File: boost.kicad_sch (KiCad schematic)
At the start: 0 parts

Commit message: Added some text in the subsheets to outline what needs to be added inside of each subsheet
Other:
- note added: "TODO: - Boost a variable voltage from the supercaps to a constant +24V - Figure out line & load regulation - Be able to shut off the boost converter with an active low signal"
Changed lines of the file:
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@@
 		(comment 1 "Robomaster")
 	)
+	(text "TODO:\n- Boost a variable voltage from the supercaps to a constant +24V\n  - Figure out line & load regulation\n- Be able to shut off the boost converter with an active low signal"
+		(exclude_from_sim no)
+		(at 125.095 90.805 0)
+		(effects
+			(font
+				(size 1.27 1.27)
+			)
+			(justify left top)
+		)
+	)
 )

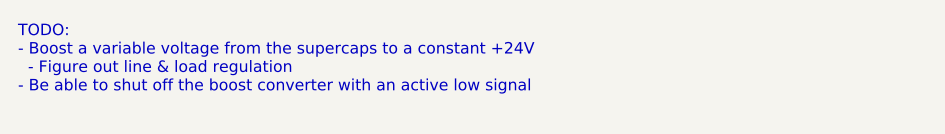
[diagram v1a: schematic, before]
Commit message: Add note about synchronous boost/buck needed
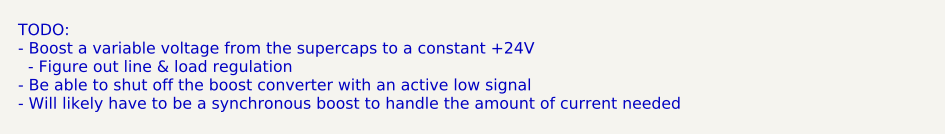
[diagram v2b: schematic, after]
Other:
- note added: "TODO: - Boost a variable voltage from the supercaps to a constant +24V - Figure out line & load regulation - Be able to shut off the boost converter with an active low signal - Will likely have to be a synchronous boost to handle the amount of current needed"
- note removed: "TODO: - Boost a variable voltage from the supercaps to a constant +24V - Figure out line & load regulation - Be able to shut off the boost converter with an active low signal"
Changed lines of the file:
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@@
 		(comment 1 "Robomaster")
 	)
-	(text "TODO:\n- Boost a variable voltage from the supercaps to a constant +24V\n  - Figure out line & load regulation\n- Be able to shut off the boost converter with an active low signal"
+	(text "TODO:\n- Boost a variable voltage from the supercaps to a constant +24V\n  - Figure out line & load regulation\n- Be able to shut off the boost converter with an active low signal\n- Will likely have to be a synchronous boost to handle the amount of current needed"
 		(exclude_from_sim no)
 		(at 125.095 90.805 0)

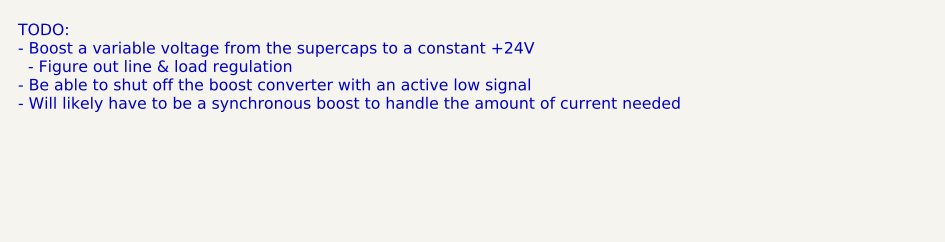
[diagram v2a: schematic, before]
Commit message: Added in & out data from each subsheet
For more details, please contact @leftisttachyon on Discord
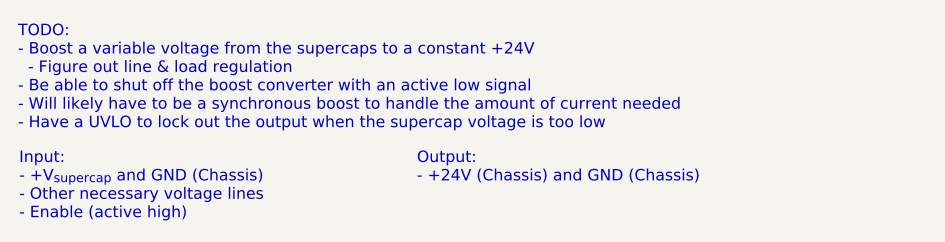
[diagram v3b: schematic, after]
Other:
- note added: "Input: - +V_{supercap} and GND (Chassis) - Other necessary voltage lines - Enable (active high)"
- note added: "Output: - +24V (Chassis) and GND (Chassis)"
- note added: "TODO: - Boost a variable voltage from the supercaps to a constant +24V - Figure out line & load regulation - Be able to shut off the boost converter with an active low signal - Will likely have to be a synchronous boost to handle the amount of current needed - Have a UVLO to lock out the output when the supercap voltage is too low"
- note removed: "TODO: - Boost a variable voltage from the supercaps to a constant +24V - Figure out line & load regulation - Be able to shut off the boost converter with an active low signal - Will likely have to be a synchronous boost to handle the amount of current needed"
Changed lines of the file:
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@@
 		(comment 1 "Robomaster")
 	)
-	(text "TODO:\n- Boost a variable voltage from the supercaps to a constant +24V\n  - Figure out line & load regulation\n- Be able to shut off the boost converter with an active low signal\n- Will likely have to be a synchronous boost to handle the amount of current needed"
+	(text "TODO:\n- Boost a variable voltage from the supercaps to a constant +24V\n  - Figure out line & load regulation\n- Be able to shut off the boost converter with an active low signal\n- Will likely have to be a synchronous boost to handle the amount of current needed\n- Have a UVLO to lock out the output when the supercap voltage is too low"
 		(exclude_from_sim no)
 		(at 125.095 90.805 0)
 		(effects
 			(font
+				(size 1.27 1.27)
+			)
+			(justify left top)
+		)
+	)
+	(text "Output:\n- +24V (Chassis) and GND (Chassis)"
+		(exclude_from_sim no)
+		(at 169.418 104.902 0)
+		(effects
+			(font
+				(size 1.27 1.27)
+			)
+			(justify left top)
+		)
+	)
+	(text "Input:\n- +V_{supercap} and GND (Chassis)\n- Other necessary voltage lines\n- Enable (active high)"
+		(exclude_from_sim no)
+		(at 125.222 104.902 0)
+		(effects
+			(font

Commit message: Completed first version of housekeeping supplies
+5V and +3V3 from mini PC +24V
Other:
- company: UT Stampede -> UT Robomaster
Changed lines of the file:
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@@
 	(paper "A4")
 	(title_block
-		(date "2024-10-18")
+		(date "2024-11-15")
 		(rev "1")
-		(company "UT Stampede")
+		(company "UT Robomaster")
 		(comment 1 "Robomaster")
 	)

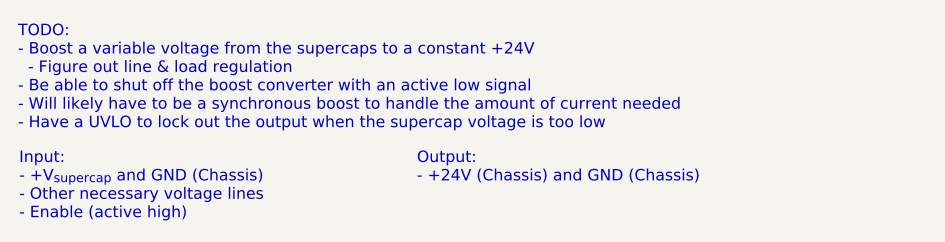
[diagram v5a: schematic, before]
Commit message: Updated sheet dates & added new subsheets for parts I forgot to include
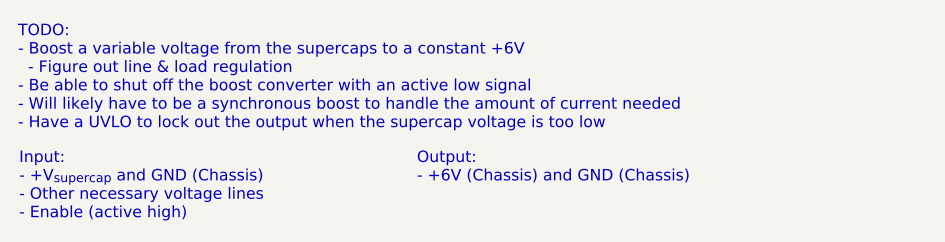
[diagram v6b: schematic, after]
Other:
- note added: "Output: - +6V (Chassis) and GND (Chassis)"
- note added: "TODO: - Boost a variable voltage from the supercaps to a constant +6V - Figure out line & load regulation - Be able to shut off the boost converter with an active low signal - Will likely have to be a synchronous boost to handle the amount of current needed - Have a UVLO to lock out the output when the supercap voltage is too low"
- note removed: "Output: - +24V (Chassis) and GND (Chassis)"
- note removed: "TODO: - Boost a variable voltage from the supercaps to a constant +24V - Figure out line & load regulation - Be able to shut off the boost converter with an active low signal - Will likely have to be a synchronous boost to handle the amount of current needed - Have a UVLO to lock out the output when the supercap voltage is too low"
- title: (none) -> Output Boost (Stage 1)
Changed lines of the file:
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@@
 	(paper "A4")
 	(title_block
-		(date "2024-12-06")
+		(title "Output Boost (Stage 1)")
+		(date "2025-02-12")
 		(rev "1")
 		(company "UT Robomaster")
 		(comment 1 "Robomaster")
 	)
-	(text "TODO:\n- Boost a variable voltage from the supercaps to a constant +24V\n  - Figure out line & load regulation\n- Be able to shut off the boost converter with an active low signal\n- Will likely have to be a synchronous boost to handle the amount of current needed\n- Have a UVLO to lock out the output when the supercap voltage is too low"
+	(text "TODO:\n- Boost a variable voltage from the supercaps to a constant +6V\n  - Figure out line & load regulation\n- Be able to shut off the boost converter with an active low signal\n- Will likely have to be a synchronous boost to handle the amount of current needed\n- Have a UVLO to lock out the output when the supercap voltage is too low"
 		(exclude_from_sim no)
 		(at 125.095 90.805 0)
@@
 		)
 	)
-	(text "Output:\n- +24V (Chassis) and GND (Chassis)"
+	(text "Output:\n- +6V (Chassis) and GND (Chassis)"
 		(exclude_from_sim no)
 		(at 169.418 104.902 0)

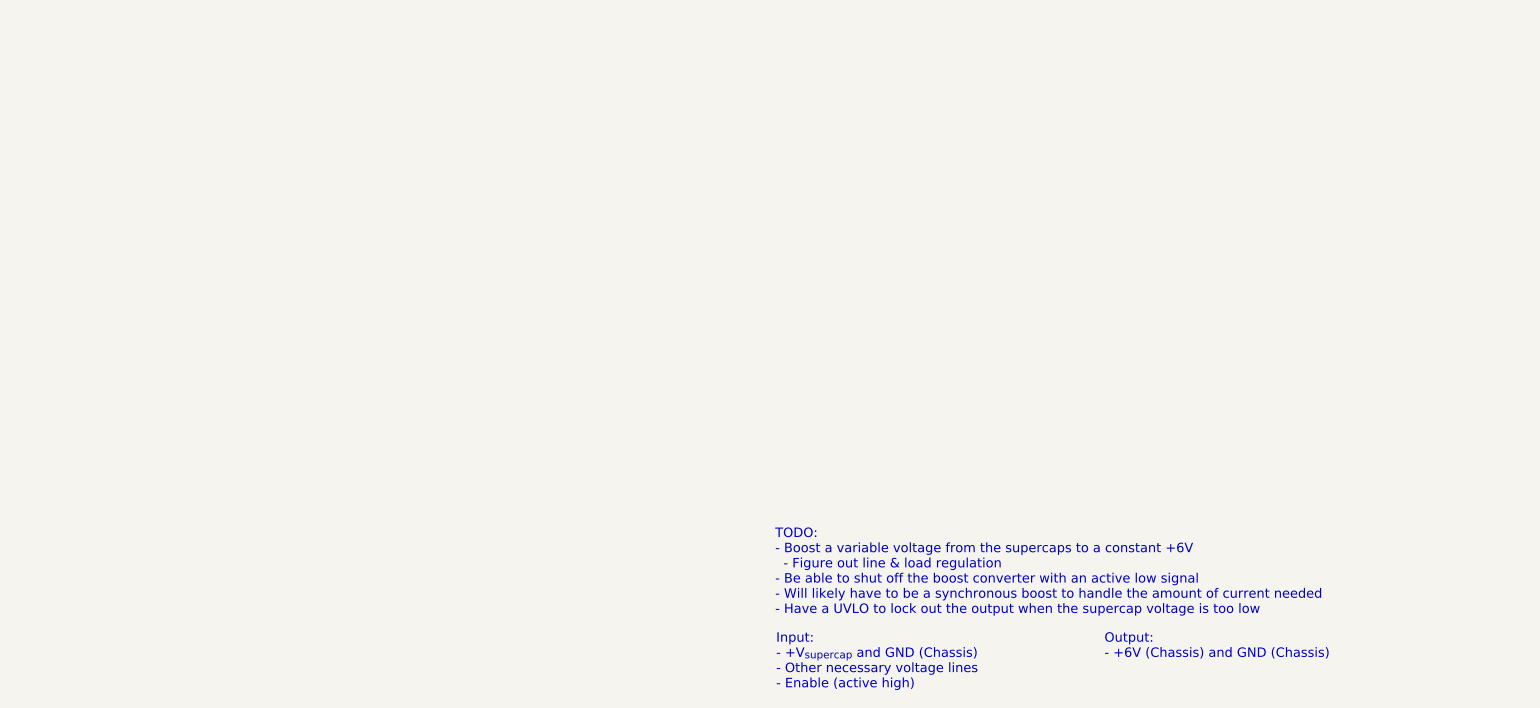
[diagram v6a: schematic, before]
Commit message: Added schematic for first stage of boost converter
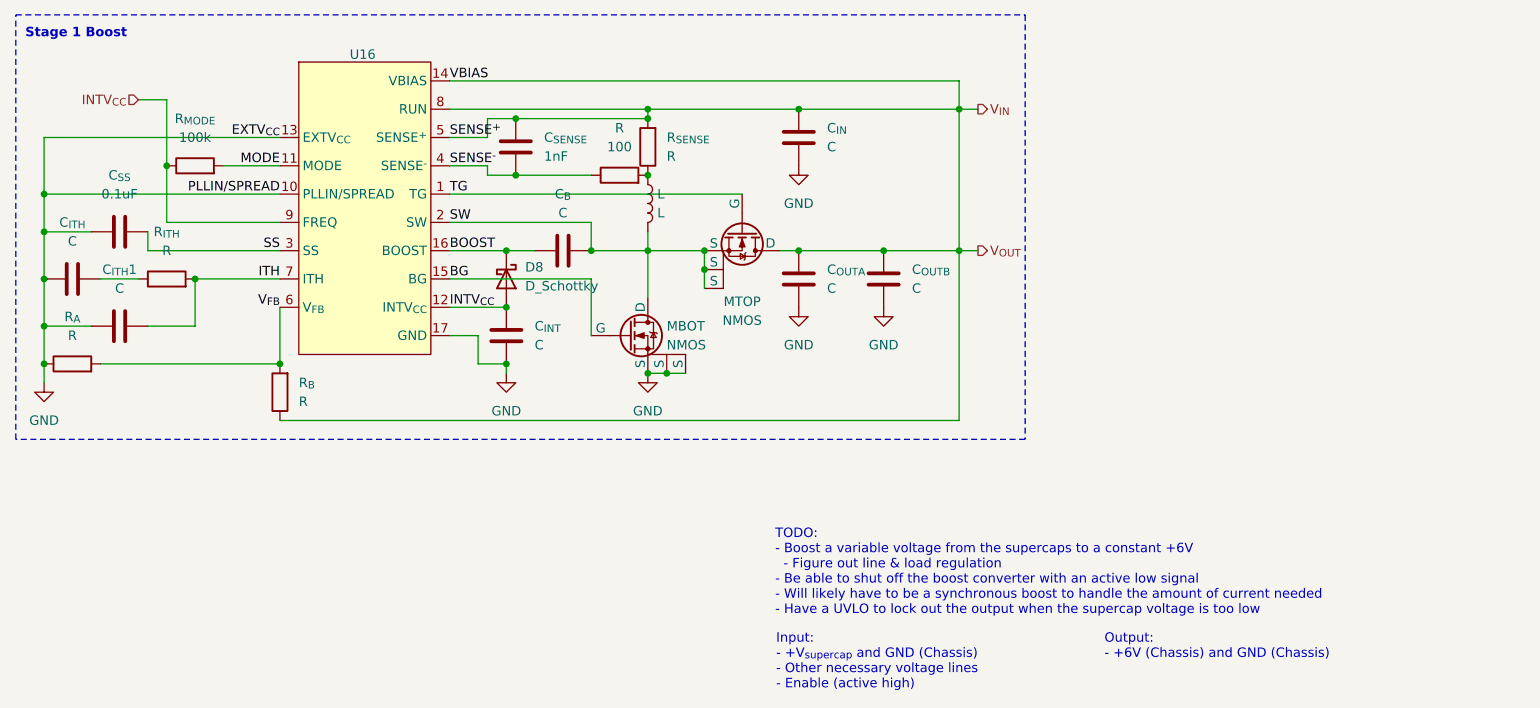
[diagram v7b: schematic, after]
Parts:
- added C_{B}, C_{INT}, C_{IN}, C_{ITH}, C_{ITH}1, C_{OUTA}, C_{OUTB}: C, symbol Device:C
- added C_{SENSE}: 1nF, symbol Device:C
- added C_{SS}: 0.1uF, symbol Device:C
- added D8: D_Schottky, symbol Device:D_Schottky
- added L: L, symbol Device:L
- added MBOT, MTOP: NMOS, Package_SON:Infineon_PG-TDSON-8_6.15x5.15mm, symbol Simulation_SPICE:NMOS
- added R: 100, symbol Device:R
- added R_{A}, R_{B}, R_{ITH}, R_{SENSE}: R, symbol Device:R
- added R_{MODE}: 100k, symbol Device:R
- added U16: ~, Package_DFN_QFN:QFN-16-1EP_3x3mm_P0.5mm_EP1.45x1.45mm, symbol ! Robomaster ICs:LTC7804
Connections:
- new net: L.1, R.2, R_{SENSE}.1
- new net: C_{ITH}.2, R_{ITH}.1
- new net BG: MBOT.4 (G), U16.15 (BG)
- new net BOOST: C_{B}.2, D8.1 (K), U16.16 (BOOST)
- new net GND: C_{INT}.1, C_{IN}.2, C_{ITH}.1, C_{ITH}1.1, C_{OUTA}.2, C_{OUTB}.2, C_{SS}.1, MBOT.1 (S), MBOT.2 (S), MBOT.3 (S), R_{A}.1, U16.10 (PLLIN/SPREAD), U16.13 (EXTV_{CC}), U16.17 (GND)
- new net INTV_{CC}: C_{INT}.2, D8.2 (A), R_{MODE}.1, U16.12 (INTV_{CC}), U16.9 (FREQ)
- new net ITH: C_{ITH}1.2, R_{ITH}.2, U16.7 (ITH)
- new net MODE: R_{MODE}.2, U16.11 (MODE)
- new net SENSE^{-}: C_{SENSE}.1, R.1, U16.4 (SENSE^{-})
- new net SS: C_{SS}.2, U16.3 (SS)
- new net SW: C_{B}.1, L.2, MBOT.5 (D), MTOP.1 (S), MTOP.2 (S), MTOP.3 (S), U16.2 (SW)
- new net TG: MTOP.4 (G), U16.1 (TG)
- new net V_{FB}: R_{A}.2, R_{B}.2, U16.6 (V_{FB})
- new net V_{IN}: C_{IN}.1, C_{OUTA}.1, C_{OUTB}.1, C_{SENSE}.2, MTOP.5 (D), R_{B}.1, R_{SENSE}.2, U16.14 (VBIAS), U16.5 (SENSE^{+}), U16.8 (RUN)
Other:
- note added: "Stage 1 Boost"
